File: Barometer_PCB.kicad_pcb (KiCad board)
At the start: 2 copper layers, 63 x 31 mm, 25 parts, among them J1 JST_Conn_01x04, U1 MS5803-01BA, U2 NPA-730B-015A, U3 24LC02

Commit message: Fix DRC checks for GND
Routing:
- net GND: vias 64 -> 69
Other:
- board text added: "3V3"
- board text added: "Dual-Barometer"
- board text added: "GND"
- board text added: "SCL"
- board text added: "SDA"
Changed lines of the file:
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@@
 		(capping no)
 		(filling no)
+		(zone_defaults)
 		(aux_axis_origin 81 111)
 		(grid_origin 81 111)
@@
 		)
 		(property "Text_Name" "PWR LED"
-			(at -2.5 0 90)
+			(at -4.25 -0.0825 0)
 			(unlocked yes)
 			(layer "F.SilkS")
 			(effects
 				(font
-					(size 0.5 0.5)
+					(size 0.75 0.75)
 					(thickness 0.125)
 					(bold yes)
@@
 		)
 		(embedded_fonts no)
-		(model "${BLESS_BAROMETER_STEPS}/MS580314BA01-00.step"
+		(model "${KIPRJMOD}/STEPS/MS580314BA01-00.step"
 			(offset
 				(xyz 0 0 3)
@@
 			)
 			(rotate
-				(xyz 0 0 0)
+				(xyz -0 -0 -0)
 			)
 		)
@@
 			(at 0.025 -3.175 90)
 			(layer "F.SilkS")
+			(hide yes)
 			(effects
 				(font
@@
 			(at 0 3.3 90)
 			(layer "F.Fab")
+			(hide yes)
 			(effects
 				(font
@@
 			)
 		)
+		(property "Text_Name" "JST Connector"
+			(at 0.025 -3.2 90)
+			(unlocked yes)
+			(layer "F.SilkS")
+			(effects
+				(font
+					(size 0.5 0.5)
+					(thickness 0.2)
+					(bold yes)
+				)
+			)
+		)
 		(property ki_fp_filters "Connector*:*_1x??_*")
 		(sheetname "/")
@@
 		(layer "Edge.Cuts")
 	)
+	(gr_text "GND"
+		(at 88.45 93.275 0)
+		(layer "F.SilkS")
+		(effects
+			(font
+				(size 0.5 0.5)
+				(thickness 0.125)
+				(bold yes)
+			)
+			(justify left bottom)
+		)
+	)
+	(gr_text "SCL"
+		(at 88.45 94.3 0)
+		(layer "F.SilkS")
+		(effects
+			(font
+				(size 0.5 0.5)
+				(thickness 0.125)
+				(bold yes)
+			)
+			(justify left bottom)
+		)
+	)
+	(gr_text "SDA"
+		(at 88.45 95.35 0)
+		(layer "F.SilkS")
+		(effects
+			(font
+				(size 0.5 0.5)
+				(thickness 0.125)
+				(bold yes)
+			)
+			(justify left bottom)
+		)
+	)
+	(gr_text "3V3"
+		(at 88.45 96.325 0)
+		(layer "F.SilkS")
+		(effects
+			(font
+				(size 0.5 0.5)
+				(thickness 0.125)
+				(bold yes)
+			)
+			(justify left bottom)
+		)
+	)
+	(gr_text "Dual-Barometer"
+		(at 92.175 83.375 0)
+		(layer "F.SilkS")
+		(effects
+			(font
+				(size 1.5 1.5)
+				(thickness 0.3)
+				(bold yes)
+			)
+			(justify left bottom)
+		)
+	)
 	(gr_text "BLESS TEAM"
 		(at 140.75 102.45 90)
@@
 	)
 	(via
+		(at 87.7 109.725)
+		(size 0.7)
+		(drill 0.33)
+		(layers "F.Cu" "B.Cu")
+		(free yes)
+		(capping no)
+		(covering
+			(front no)
+			(back no)
+		)
+		(plugging
+			(front no)
+			(back no)
+		)
+		(filling no)
+		(net "GND")
+	)
+	(via
 		(at 121.7 100.25)
 		(size 0.7)
@@
 	)
 	(via
-		(at 131.2675 88.15)
+		(at 131.25 88.15)
 		(size 0.7)
 		(drill 0.33)
@@
 	)
 	(via
+		(at 88.825 107.025)
+		(size 0.7)
+		(drill 0.33)
+		(layers "F.Cu" "B.Cu")
+		(free yes)
+		(capping no)
+		(covering
+			(front no)
+			(back no)
+		)
+		(plugging
+			(front no)
+			(back no)
+		)
+		(filling no)
+		(net "GND")
+	)
+	(via
+		(at 82.275 104.275)
+		(size 0.7)
+		(drill 0.33)
+		(layers "F.Cu" "B.Cu")
+		(free yes)
+		(capping no)
+		(covering
+			(front no)
+			(back no)
+		)
+		(plugging
+			(front no)
+			(back no)
+		)
+		(filling no)
+		(net "GND")
+	)
+	(via
 		(at 127 94.75)
 		(size 0.7)
@@
 	)
 	(via
+		(at 85 103.15)
+		(size 0.7)
+		(drill 0.33)
+		(layers "F.Cu" "B.Cu")
+		(free yes)
+		(capping no)
+		(covering
+			(front no)
+			(back no)
+		)
+		(plugging
+			(front no)
+			(back no)
+		)
+		(filling no)
+		(net "GND")
+	)
+	(via
 		(at 121.695445 96.740907)
 		(size 0.7)
@@
 	)
 	(via
+		(at 87.725 104.3)
+		(size 0.7)
+		(drill 0.33)
+		(layers "F.Cu" "B.Cu")
+		(free yes)
+		(capping no)
+		(covering
+			(front no)
+			(back no)
+		)
+		(plugging
+			(front no)
+			(back no)
+		)
+		(filling no)
+		(net "GND")
+	)
+	(via
 		(at 91.155457 89.204742)
 		(size 0.7)
@@
 	(segment
 		(start 126.3 90.8)
-		(end 128.5 93)
+		(end 128.575 93.075)
 		(width 0.5)
 		(layer "F.Cu")
@@
 	)
 	(segment
-		(start 120.195 93.505)
-		(end 120.195 91.405)
+		(start 131.8925 94.0925)
+		(end 131.8925 95.574998)
 		(width 0.5)
 		(layer "F.Cu")
@@
 	)
 	(segment
-		(start 120.8 90.8)
-		(end 126.3 90.8)
-		(width 0.5)
-		(layer "F.Cu")
-		(net "/I2C_SDA")
-	)
-	(segment
-		(start 95.0175 95.7375)
-		(end 96.605 95.7375)
-		(width 0.5)
-		(layer "F.Cu")
-		(net "/I2C_SDA")
-	)
-	(segment
 		(start 120.195 91.405)
 		(end 120.8 90.8)
@@
 	)
 	(segment
-		(start 131.8925 94.0925)
-		(end 131.8925 95.574998)
+		(start 95.0175 95.7375)
+		(end 96.605 95.7375)
 		(width 0.5)
 		(layer "F.Cu")
@@
 	)
 	(segment
-		(start 130.8 93)
-		(end 131.8925 94.0925)
-		(width 0.5)
-		(layer "F.Cu")
-		(net "/I2C_SDA")
-	)
-	(segment
-		(start 128.5 93)
-		(end 130.8 93)
+		(start 128.575 93.075)
+		(end 130.875 93.075)
 		(width 0.5)
 		(layer "F.Cu")
@@
 	)
 	(segment
+		(start 120.195 93.505)
+		(end 120.195 91.405)
+		(width 0.5)
+		(layer "F.Cu")
+		(net "/I2C_SDA")
+	)
+	(segment
+		(start 130.875 93.075)
+		(end 131.8925 94.0925)
+		(width 0.5)
+		(layer "F.Cu")
+		(net "/I2C_SDA")
+	)
+	(segment
 		(start 119.1 102.15)
 		(end 120.195 101.055)
@@
 		(width 0.5)
 		(layer "F.Cu")
+		(net "/I2C_SDA")
+	)
+	(segment
+		(start 120.8 90.8)
+		(end 126.3 90.8)
+		(width 0.5)
+		(layer "F.Cu")

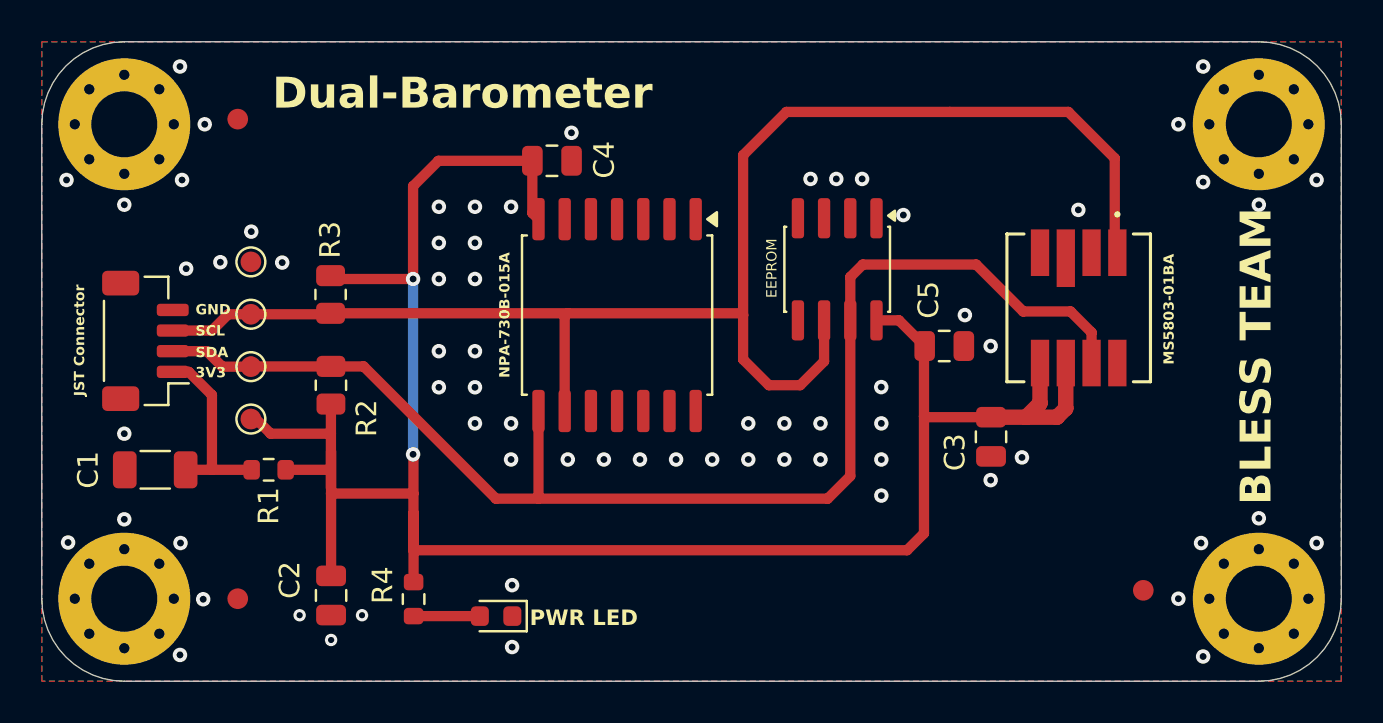
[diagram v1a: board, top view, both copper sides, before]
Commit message: JST pin and test point texts
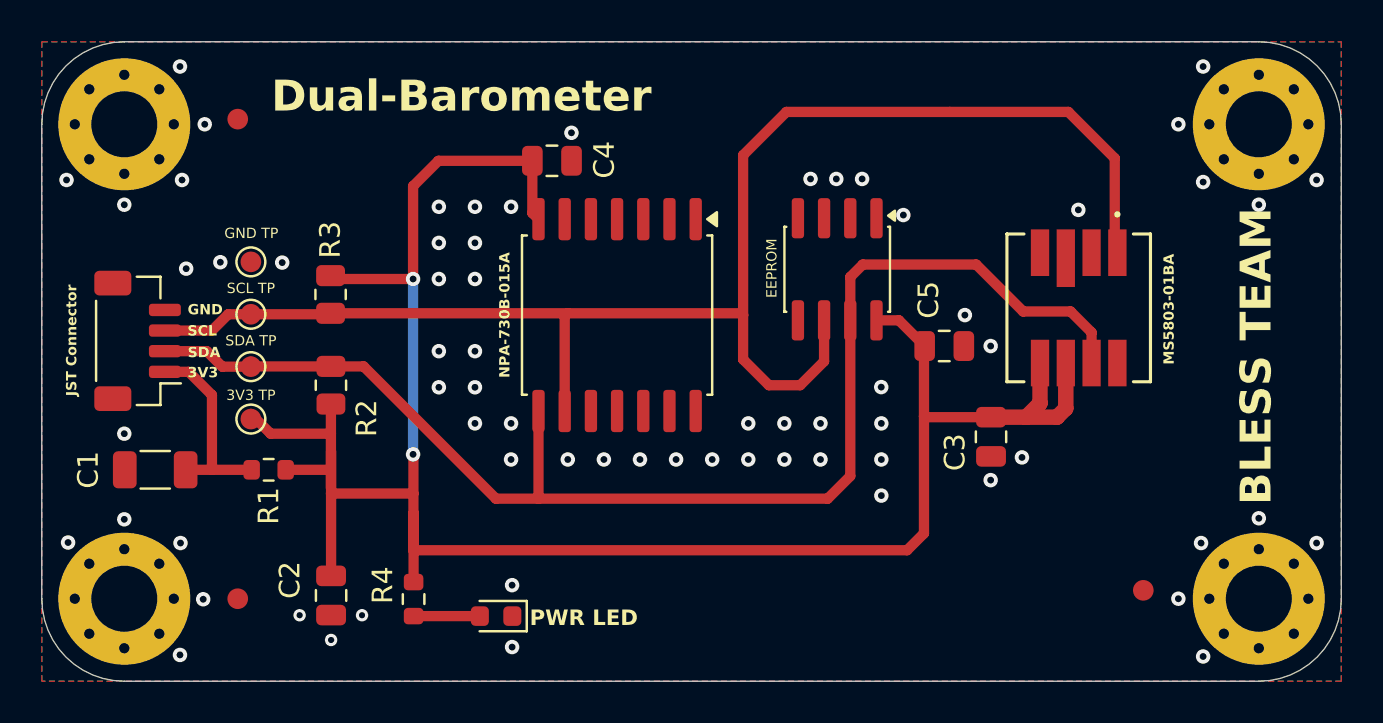
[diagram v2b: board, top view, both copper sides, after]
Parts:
- moved J1 0.38 mm to (85.6, 94.5)
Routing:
- net GND: vias 69 -> 68
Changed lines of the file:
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@@
 	(title_block
 		(title "Dual-Barometer Pressure Measurement System")
-		(date "2026-06-11")
+		(date "2026-06-14")
 		(rev "A")
 		(company "BLESS - Universidad Francisco de Vitoria")
@@
 		(capping no)
 		(filling no)
-		(zone_defaults)
 		(aux_axis_origin 81 111)
 		(grid_origin 81 111)
@@
 			(at 0 1.55 0)
 			(layer "F.Fab")
+			(hide yes)
 			(effects
 				(font
@@
 			)
 		)
+		(property "Text_Name" "SCL TP"
+			(at 0 1.26 0)
+			(unlocked yes)
+			(layer "F.SilkS")
+			(effects
+				(font
+					(size 0.5 0.5)
+					(thickness 0.125)
+				)
+			)
+		)
 		(property ki_fp_filters "Pin* Test*")
 		(sheetname "/")
@@
 			(at 0 1.55 90)
 			(layer "F.Fab")
+			(hide yes)
 			(effects
 				(font
@@
 			)
 		)
+		(property "Text_Name" "3V3 TP"
+			(at -1.1584 0 0)
+			(unlocked yes)
+			(layer "F.SilkS")
+			(effects
+				(font
+					(size 0.5 0.5)
+					(thickness 0.125)
+				)
+			)
+		)
 		(property ki_fp_filters "Pin* Test*")
 		(sheetname "/")
@@
 			(at 0 1.55 0)
 			(layer "F.Fab")
+			(hide yes)
 			(effects
 				(font
@@
 			)
 		)
+		(property "Text_Name" "GND TP"
+			(at 0.0225 -1.387 0)
+			(unlocked yes)
+			(layer "F.SilkS")
+			(effects
+				(font
+					(size 0.5 0.5)
+					(thickness 0.15)
+				)
+			)
+		)
 		(attr exclude_from_pos_files)
 		(duplicate_pad_numbers_are_jumpers no)
@@
 			(at 0 1.55 0)
 			(layer "F.Fab")
+			(hide yes)
 			(effects
 				(font
@@
 			)
 		)
+		(property "Text_Name" "SDA TP"
+			(at 0 1.26 0)
+			(unlocked yes)
+			(layer "F.SilkS")
+			(effects
+				(font
+					(size 0.5 0.5)
+					(thickness 0.125)
+				)
+			)
+		)
 		(property ki_fp_filters "Pin* Test*")
 		(sheetname "/")
@@
 	(footprint "Connector_JST:JST_SH_BM04B-SRSS-TB_1x04-1MP_P1.00mm_Vertical"
 		(layer "F.Cu")
-		(at 86.025 94.5 90)
+		(at 85.644 94.5 90)
 		(descr "JST SH series connector, BM04B-SRSS-TB (http://www.jst-mfg.com/product/pdf/eng/eSH.pdf), generated with kicad-footprint-generator")
 		(tags "connector JST SH vertical")
@@
 		(layer "Edge.Cuts")
 	)
-	(gr_text "GND"
-		(at 88.45 93.275 0)
+	(gr_text "SCL"
+		(at 88.0612 94.3 0)
 		(layer "F.SilkS")
 		(effects
@@
 		)
 	)
-	(gr_text "SCL"
-		(at 88.45 94.3 0)
+	(gr_text "GND"
+		(at 88.069 93.275 0)
 		(layer "F.SilkS")
 		(effects
@@
 	)
 	(gr_text "SDA"
-		(at 88.45 95.35 0)
+		(at 88.069 95.35 0)
 		(layer "F.SilkS")
 		(effects
@@
 	)
 	(gr_text "3V3"
-		(at 88.45 96.325 0)
+		(at 88.069 96.325 0)
 		(layer "F.SilkS")
 		(effects
@@
 	)
 	(gr_text "Dual-Barometer"
-		(at 92.175 83.375 0)
+		(at 92.1252 83.5172 0)
 		(layer "F.SilkS")
 		(effects
@@
 	)
 	(via
-		(at 91.155457 89.204742)
-		(size 0.7)
-		(drill 0.33)
-		(layers "F.Cu" "B.Cu")
-		(free yes)
-		(capping no)
-		(covering
-			(front no)
-			(back no)
-		)
-		(plugging
-			(front no)
-			(back no)
-		)
-		(filling no)
-		(net "GND")
-	)
-	(via
 		(at 106.5 100.25)
 		(size 0.7)
@@
 	)
 	(segment
-		(start 106.5 93.1625)
-		(end 106.35 93.3125)
+		(start 86.969 94)
+		(end 88.869 94)
 		(width 0.5)
 		(layer "F.Cu")
@@
 	)
 	(segment
-		(start 114.9125 93.1625)
-		(end 115 93.25)
+		(start 106.5 93.1625)
+		(end 106.35 93.3125)
 		(width 0.5)
 		(layer "F.Cu")
@@
 	)
 	(segment
-		(start 87.35 94)
-		(end 89.25 94)
+		(start 114.9125 93.1625)
+		(end 115 93.25)
 		(width 0.5)
 		(layer "F.Cu")
@@
 	)
 	(segment
-		(start 133.0165 85.649)
-		(end 133.0165 90.225002)
+		(start 88.869 94)
+		(end 89.25 94)
 		(width 0.5)
 		(layer "F.Cu")
@@
 	)
 	(segment
-		(start 89.25 94)
-		(end 90.04 93.21)
+		(start 133.0165 85.649)
+		(end 133.0165 90.225002)
 		(width 0.5)
 		(layer "F.Cu")
@@
 	)
 	(segment
-		(start 90.04 93.21)
-		(end 91.1375 93.21)
-		(width 0.5)
-		(layer "F.Cu")
-		(net "/I2C_SCL")
-	)
-	(segment
 		(start 115 95.4)
 		(end 116.25 96.65)
@@
 	)
 	(segment
+		(start 90.04 93.21)
+		(end 91.1375 93.21)
+		(width 0.5)
+		(layer "F.Cu")
+		(net "/I2C_SCL")
+	)
+	(segment
+		(start 89.25 94)
+		(end 90.04 93.21)
+		(width 0.5)
+		(layer "F.Cu")
+		(net "/I2C_SCL")
+	)
+	(segment
 		(start 117.1 83.4)
 		(end 115 85.5)
@@
 	)
 	(segment
-		(start 89.75 95.75)
-		(end 89 95)
+		(start 91.1375 95.75)
+		(end 89.75 95.75)
 		(width 0.5)
 		(layer "F.Cu")
@@
 	)
 	(segment
-		(start 91.1375 95.75)
-		(end 89.75 95.75)
-		(width 0.5)
-		(layer "F.Cu")
-		(net "/I2C_SDA")
-	)
-	(segment
 		(start 91.1375 95.5)
 		(end 91.375 95.7375)
@@
 	)
 	(segment
-		(start 128.575 93.075)
-		(end 130.875 93.075)
+		(start 89.75 95.75)
+		(end 89 95)
 		(width 0.5)
 		(layer "F.Cu")
@@
 	)
 	(segment
-		(start 89 95)
-		(end 87.35 95)
+		(start 128.575 93.075)
+		(end 130.875 93.075)
 		(width 0.5)
 		(layer "F.Cu")
@@
 	)
 	(segment
+		(start 89 95)
+		(end 87.35 95)
+		(width 0.5)
+		(layer "F.Cu")
+		(net "/I2C_SDA")
+	)
+	(segment
 		(start 130.875 93.075)
 		(end 131.8925 94.0925)
@@
 	)
 	(segment
-		(start 88.124999 96)
-		(end 89.25 97.125001)
+		(start 89.25 97.125001)
+		(end 89.25 100.75)
 		(width 0.5)
 		(layer "F.Cu")
@@
 	)
 	(segment
-		(start 87.35 96)
+		(start 86.969 96)
 		(end 88.124999 96)
 		(width 0.5)
@@
 	)
 	(segment
-		(start 89.25 97.125001)
-		(end 89.25 100.75)
+		(start 89.25 100.75)
+		(end 87.975 100.75)
 		(width 0.5)
 		(layer "F.Cu")
@@
 	)
 	(segment
-		(start 89.25 100.75)
-		(end 87.975 100.75)
+		(start 91.175 100.75)
+		(end 89.25 100.75)
 		(width 0.5)
 		(layer "F.Cu")
@@
 	)
 	(segment
-		(start 91.175 100.75)
-		(end 89.25 100.75)
+		(start 88.124999 96)
+		(end 89.25 97.125001)
 		(width 0.5)
 		(layer "F.Cu")
